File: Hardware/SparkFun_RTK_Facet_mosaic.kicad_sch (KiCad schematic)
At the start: 27 parts, among them J3 Qwiic_RA, J5 Conn_01x12_FPC_0.5mm, J6 Conn_01x12_FPC_0.5mm, J7 Conn_01x12_FPC_0.5mm, U1 ESP32-WROVER-E-N16R8

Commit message: v1.2 routed
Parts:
- removed J5, J6, J7: Conn_01x12_FPC_0.5mm, SparkFun-Connector:FPC_0.5mm-12, symbol SparkFun-Connector:Conn_01x12_FPC_0.5mm
- added J4: Conn_01x12, SparkFun-Connector:JST_SMD_1.0mm-12_RA, symbol SparkFun-Connector:Conn_01x12_JST_RA
- added J5: Conn_01x14, SparkFun-Connector:JST_SMD_1.0mm-14_RA, symbol SparkFun-Connector:Conn_01x14_JST_RA
- D2: value TVS_ESD_4_HS -> DF5A5.6LFU
- FID1, FID2, FID3, FID4: value Fiducial_0.5 -> Fiducial_0.5mm
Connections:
- net 3.3V_P: now also J4.3 (Pin_3), J4.4 (Pin_4), J5.8 (Pin_8)
- net ESP21/SDA: now also J4.10 (Pin_10), J5.7 (Pin_7)
- net ESP22/SCL: now also J4.9 (Pin_9), J5.6 (Pin_6)
- net ExternalDATA_RXI: now also J5.4 (Pin_4)
- net ExternalDATA_TXO: now also J5.5 (Pin_5)
- net GND: now also J4.1 (Pin_1), J5.13 (Pin_13), J5.14 (Pin_14)
- net MRX2: now also J5.11 (Pin_11)
- net MTX2: now also J5.12 (Pin_12)
- net POWER_BTN: now also J4.2 (Pin_2)
- net SD_CLK: now also J4.7 (Pin_7)
- net SD_CMD: now also J4.6 (Pin_6)
- net SD_DATA: now also J4.8 (Pin_8)
- net USB_DM: now also J5.10 (Pin_10)
- net USB_DP: now also J5.9 (Pin_9)
- net VRAW: now also J5.3 (Pin_3)
- net VUSB: now also J4.12 (Pin_12), J5.1 (Pin_1), J5.2 (Pin_2)
- net at D2.3 (K2), R28.2: now also J4.5 (Pin_5)
- net at J3.NC1 (NC): no longer J3.NC2 (NC)
- net ESP19/CHG_LED2 renamed ESP19/CHG_STAT2
- net ESP34/CHG_LED renamed ESP34/CHG_STAT1
- new net CHG_LED: J4.11 (Pin_11)
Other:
- title: RTK Facet L-Band mosaic -> RTK Facet mosaic L-Band
- moved on the sheet: TP13

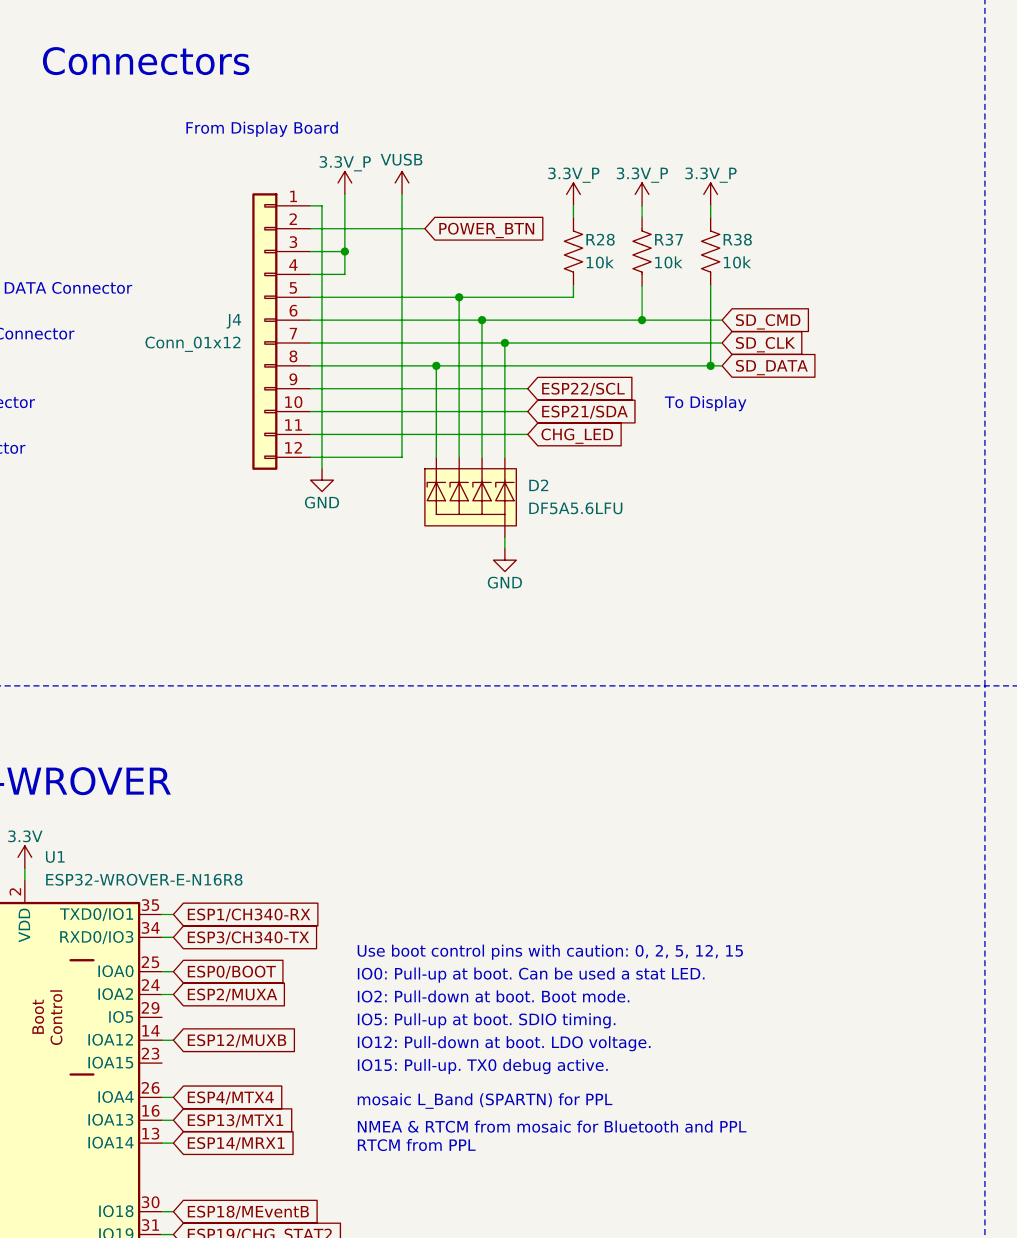
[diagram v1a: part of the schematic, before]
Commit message: Add SD_DET and 1A regulator
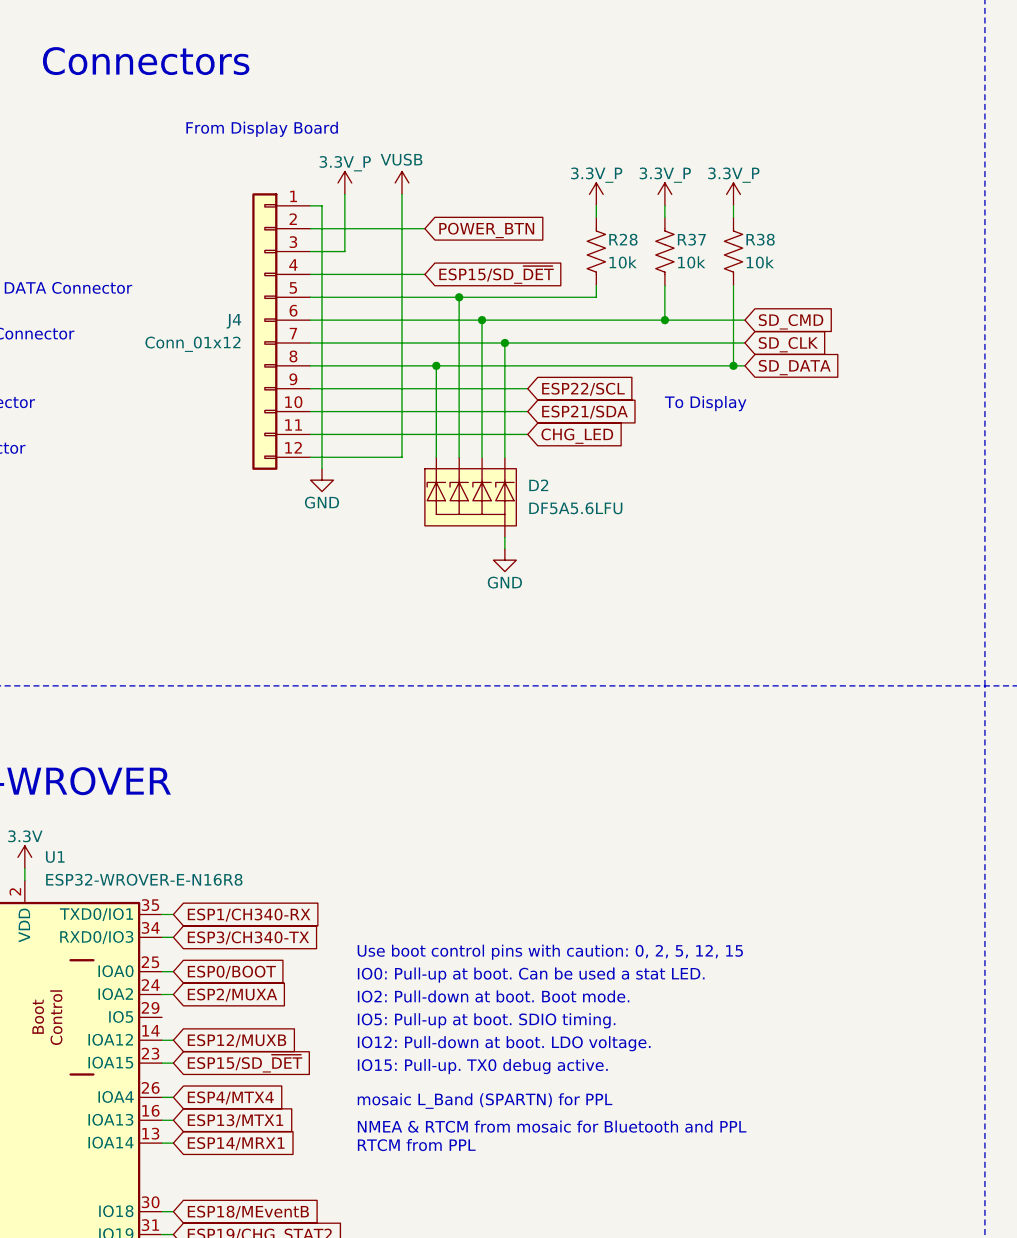
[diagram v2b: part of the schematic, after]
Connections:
- net 3.3V_P: no longer J4.4 (Pin_4)
- net ESP15/SD_~{DET}: now reaches U1.23 (IOA15)
- net ESP15/SD_~{DET}: now also J4.4 (Pin_4)
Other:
- moved on the sheet: R28, R37, R38

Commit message: Add JST PROD_IDs. Update AP7361C regulator
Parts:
- J4: PROD_ID ... -> CONN-23694
- J5: PROD_ID ... -> CONN-23695
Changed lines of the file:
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@@
 			)
 		)
-		(property "PROD_ID" "..."
+		(property "PROD_ID" "CONN-23694"
 			(at 106.68 77.47 0)
 			(effects
@@
 			)
 		)
-		(property "PROD_ID" "..."
+		(property "PROD_ID" "CONN-23695"
 			(at 45.72 82.55 0)
 			(effects
